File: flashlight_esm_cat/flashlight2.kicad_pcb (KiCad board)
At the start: 2 copper layers, 49.3 x 50.8 mm, 6 parts, among them SW1 SW_SPST

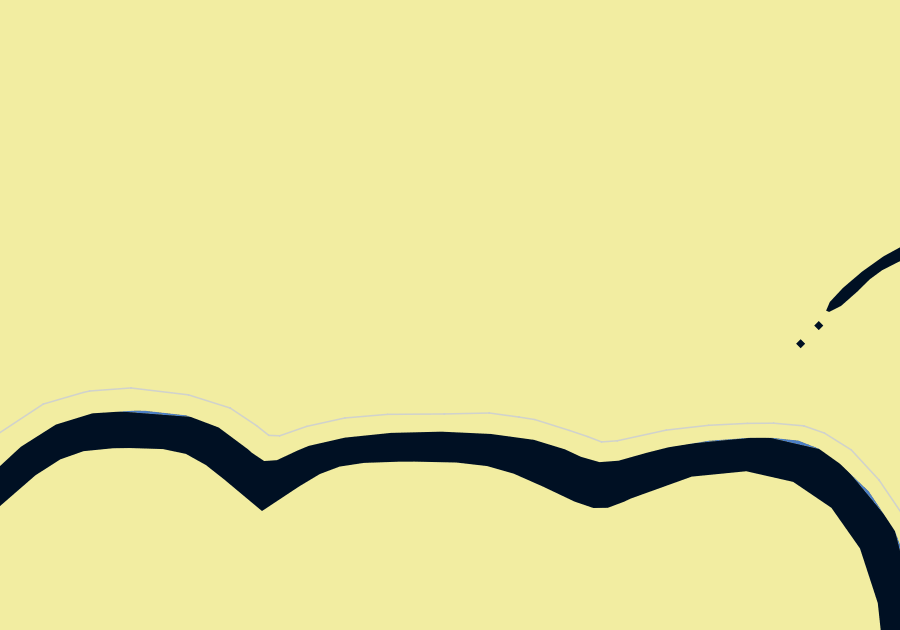
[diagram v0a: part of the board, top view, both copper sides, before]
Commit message: feat: flashlight add keychain hole
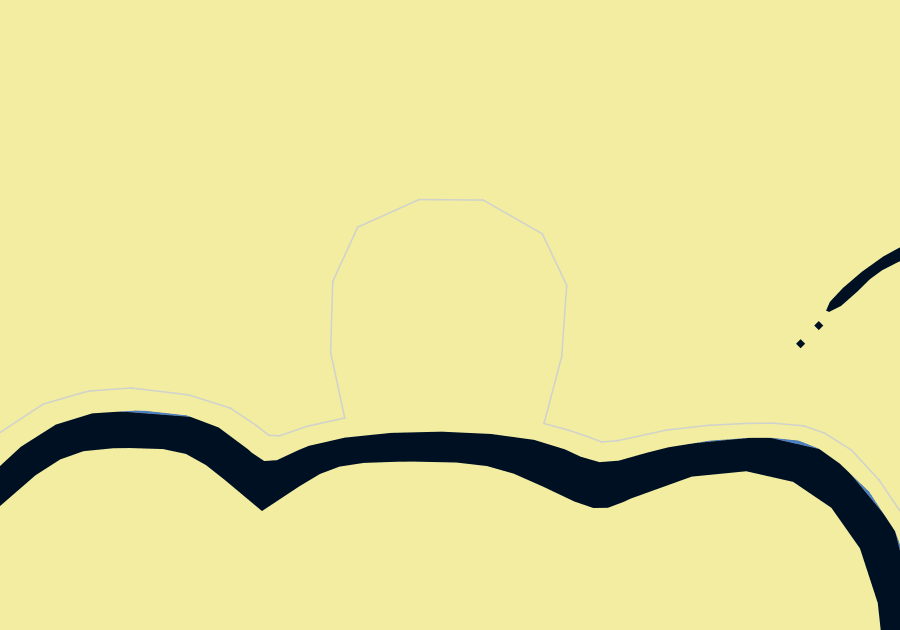
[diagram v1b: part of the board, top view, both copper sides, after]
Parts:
- added ?: , , F.Cu at (188.4, 71.8)
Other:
- board size 49.3 x 50.8 mm -> 49.3 x 57.1 mm
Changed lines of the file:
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@@
 		)
 	)
+	(footprint ""
+		(layer "F.Cu")
+		(at 188.391595 71.840666)
+		(property "Reference" ""
+			(at 0 0 0)
+			(layer "F.SilkS")
+			(effects
+				(font
+					(size 1.27 1.27)
+					(thickness 0.15)
+				)
+			)
+		)
+		(property "Value" ""
+			(at 0 0 0)
+			(layer "F.Fab")
+			(effects
+				(font
+					(size 1.27 1.27)
+					(thickness 0.15)
+				)
+			)
+		)
+		(property "Footprint" ""
+			(at 0 0 0)
+			(layer "F.Fab")
+			(hide yes)
+			(effects
+				(font
+					(size 1.27 1.27)
+					(thickness 0.15)
+				)
+			)
+		)
+		(property "Datasheet" ""
+			(at 0 0 0)
+			(layer "F.Fab")
+			(hide yes)
+			(effects
+				(font
+					(size 1.27 1.27)
+					(thickness 0.15)
+				)
+			)
+		)
+		(property "Description" ""
+			(at 0 0 0)
+			(layer "F.Fab")
+			(hide yes)
+			(effects
+				(font
+					(size 1.27 1.27)
+					(thickness 0.15)
+				)
+			)
+		)
+		(pad "1" thru_hole circle
+			(at 0 0)
+			(size 6.4 6.4)
+			(drill 3.2)
+			(layers "*.Cu" "*.Mask")
+			(remove_unused_layers no)
+		)
+	)
 	(footprint "LED_THT:LED_D3.0mm"
 		(layer "F.Cu")
@@
 		(fp_arc
 			(start 0.95 3.05)
-			(mid 1.371575 3.178399)
+			(mid 1.371573 3.1784)
 			(end 1.65 3.52)
 			(stroke
@@
 		(fp_arc
 			(start 0.95 3.3)
-			(mid 1.22459 3.381628)
+			(mid 1.224591 3.381627)
 			(end 1.41 3.6)
 			(stroke
@@
 			(xy 176.491956 74.372021) (xy 177.869105 74.27001) (xy 179.788186 74.499535) (xy 181.179616 74.939458)
 			(xy 182.059461 75.526021) (xy 182.467505 75.851181) (xy 182.83092 75.863932) (xy 183.729891 75.551524)
-			(xy 184.998653 75.270993) (xy 186.426807 75.149855) (xy 188.320386 75.137104) (xy 189.818673 75.105226)
-			(xy 190.804794 75.240353) (xy 191.333976 75.323237) (xy 192.487976 75.686651) (xy 193.093666 75.890673)
+			(xy 184.998653 75.270993) (xy 184.526231 73.076621) (xy 184.599959 70.717352) (xy 185.429389 68.911036)
+			(xy 187.475318 67.989447) (xy 189.613405 68.007879) (xy 191.585606 69.132218) (xy 192.396605 70.846374)
+			(xy 192.230719 73.224075) (xy 191.640902 75.454321) (xy 192.487976 75.686651) (xy 193.093666 75.890673)
 			(xy 193.559091 76.069193) (xy 194.081898 76.030938) (xy 195.720449 75.6739) (xy 197.129476 75.514508)
 			(xy 198.417365 75.450751) (xy 199.29721 75.444375) (xy 200.298193 75.533635) (xy 200.986292 75.772723)

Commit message: feat: labelling etc.
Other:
- board text added: "JLCJLCJLCJLC"
- board text added: "by Justin & Hackin7"
- board text added: "maibadge: flashlight cat"
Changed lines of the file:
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@@
 		(attr through_hole)
-		(fp_line
-			(start 0.95 -3.05)
-			(end -1.5 -3.05)
-			(stroke
-				(width 0.12)
-				(type solid)
-			)
-			(layer "B.SilkS")
-		)
-		(fp_line
-			(start -1.5 3.05)
-			(end 0.95 3.05)
-			(stroke
-				(width 0.12)
-				(type solid)
-			)
-			(layer "B.SilkS")
-		)
-		(fp_line
-			(start -2.05 -2.5)
-			(end -2.05 2.5)
-			(stroke
-				(width 0.12)
-				(type solid)
-			)
-			(layer "B.SilkS")
-		)
-		(fp_arc
-			(start 29.2 0)
-			(mid 16.974433 13.886953)
-			(end 1.65 3.52)
-			(stroke
-				(width 0.12)
-				(type solid)
-			)
-			(layer "B.SilkS")
-		)
-		(fp_arc
-			(start 1.65 -3.52)
-			(mid 16.974433 -13.886954)
-			(end 29.2 0)
-			(stroke
-				(width 0.12)
-				(type solid)
-			)
-			(layer "B.SilkS")
-		)
-		(fp_arc
-			(start 1.65 -3.52)
-			(mid 1.371574 -3.178401)
-			(end 0.95 -3.05)
-			(stroke
-				(width 0.12)
-				(type solid)
-			)
-			(layer "B.SilkS")
-		)
-		(fp_arc
-			(start 0.95 3.05)
-			(mid 1.371573 3.1784)
-			(end 1.65 3.52)
-			(stroke
-				(width 0.12)
-				(type solid)
-			)
-			(layer "B.SilkS")
-		)
-		(fp_arc
-			(start -1.5 3.05)
-			(mid -1.888909 2.888909)
-			(end -2.05 2.5)
-			(stroke
-				(width 0.12)
-				(type solid)
-			)
-			(layer "B.SilkS")
-		)
-		(fp_arc
-			(start -2.05 -2.5)
-			(mid -1.888909 -2.888909)
-			(end -1.5 -3.05)
-			(stroke
-				(width 0.12)
-				(type solid)
-			)
-			(layer "B.SilkS")
-		)
 		(fp_line
 			(start 0.95 -3.3)
@@
 		(layer "Edge.Cuts")
 	)
+	(gr_text "by Justin & Hackin7"
+		(at 201.47282 83.290135 0)
+		(layer "B.SilkS")
+		(effects
+			(font
+				(size 1.54 1.54)
+				(thickness 0.25)
+				(bold yes)
+			)
+			(justify left bottom mirror)
+		)
+	)
+	(gr_text "maibadge: flashlight cat"
+		(at 201.286198 80.490807 0)
+		(layer "B.SilkS")
+		(effects
+			(font
+				(size 1.54 1.54)
+				(thickness 0.25)
+				(bold yes)
+			)
+			(justify left bottom mirror)
+		)
+	)
+	(gr_text "JLCJLCJLCJLC"
+		(at 193.696909 101.454662 0)
+		(layer "B.SilkS")
+		(effects
+			(font
+				(size 1.54 1.54)
+				(thickness 0.25)
+				(bold yes)
+			)
+			(justify left bottom mirror)
+		)
+	)
 	(segment
